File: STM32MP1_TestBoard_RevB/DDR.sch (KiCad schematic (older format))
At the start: 18 parts, among them U1 STM32MP157xAB, U2 MT41K256M16TW-107

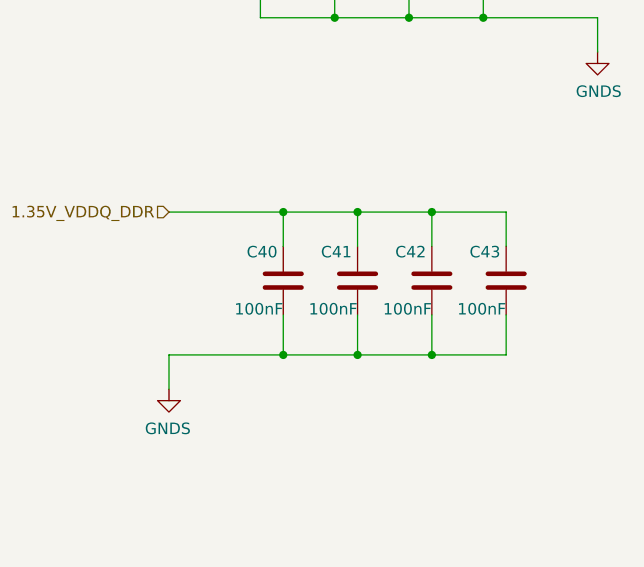
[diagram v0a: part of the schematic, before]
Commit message: Removed 1.35V led and unused DDR capacitors
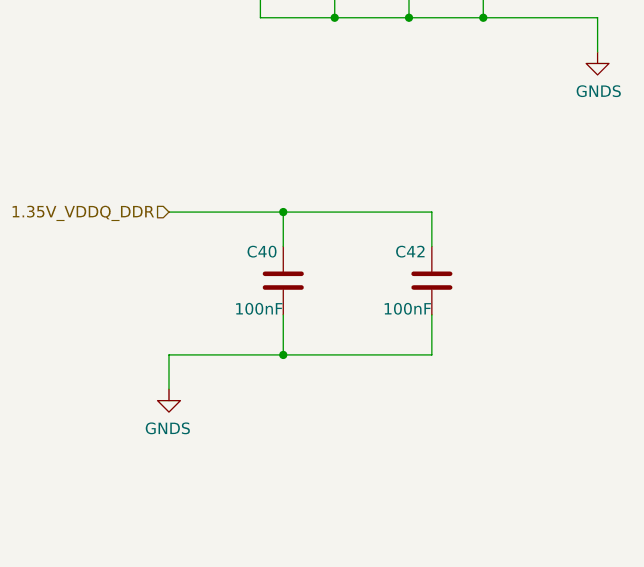
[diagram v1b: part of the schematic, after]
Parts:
- removed C41, C43: 100nF, Capacitor_SMD:C_0402_1005Metric_Pad0.74x0.62mm_HandSolder, symbol Device:C
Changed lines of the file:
@@
 	12825 3425 12500 3425
-Wire Wire Line
-	13250 5050 13250 4900
-$Comp
-L Device:C C43
-U 1 1 60C8F78E
-P 13250 5200
-F 0 "C43" H 13275 5325 50  0000 L CNN
-F 1 "100nF" H 13250 5075 50  0000 L CNN
-F 2 "Capacitor_SMD:C_0402_1005Metric_Pad0.74x0.62mm_HandSolder" H 13288 5050 50  0001 C CNN
-F 3 "~" H 13250 5200 50  0001 C CNN
-F 4 "~" H 13250 5200 50  0001 C CNN "Mfr"
-F 5 "~" H 13250 5200 50  0001 C CNN "PartNo"
-	1    13250 5200
-	-1   0    0    -1
-$EndComp
-Wire Wire Line
-	13250 5350 13250 5525
 Wire Wire Line
 	12925 5050 12925 4900
@@
 	12925 5350 12925 5525
 Wire Wire Line
-	12600 5050 12600 4900
-$Comp
-L Device:C C41
-U 1 1 60C8F79E
-P 12600 5200
-F 0 "C41" H 12625 5325 50  0000 L CNN
-F 1 "100nF" H 12600 5075 50  0000 L CNN
-F 2 "Capacitor_SMD:C_0402_1005Metric_Pad0.74x0.62mm_HandSolder" H 12638 5050 50  0001 C CNN
-F 3 "~" H 12600 5200 50  0001 C CNN
-F 4 "~" H 12600 5200 50  0001 C CNN "Mfr"
-F 5 "~" H 12600 5200 50  0001 C CNN "PartNo"
-	1    12600 5200
-	-1   0    0    -1
-$EndComp
-Wire Wire Line
-	12600 5350 12600 5525
-Wire Wire Line
 	12275 5050 12275 4900
 $Comp
@@
 Wire Wire Line
 	12275 5350 12275 5525
-Wire Wire Line
-	13250 4900 12925 4900
-Connection ~ 12925 4900
-Wire Wire Line
-	12925 4900 12600 4900
-Connection ~ 12600 4900
-Wire Wire Line
-	12600 4900 12275 4900
 Connection ~ 12275 4900
 Wire Wire Line
@@
 Wire Wire Line
 	11775 5525 11775 5675
-Wire Wire Line
-	13250 5525 12925 5525
-Connection ~ 12925 5525
-Wire Wire Line
-	12925 5525 12600 5525
-Connection ~ 12600 5525
-Wire Wire Line
-	12600 5525 12275 5525
 Connection ~ 12275 5525
 Wire Wire Line
@@
 NoConn ~ 4700 5625
 NoConn ~ 4700 5725
+Wire Wire Line
+	12275 5525 12925 5525
+Wire Wire Line
+	12275 4900 12925 4900
 $EndSCHEMATC

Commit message: Updated design
- Added Crystal/Oscillators
- Replaced both SDMMC with single SDMMC w/ detect pin
- Added USB Type C for VIN
- Moved SWD pins
- Tidied up silk screen for pin headers J1, J2, J3, J4
- Moved DSI socket
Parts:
- C36, C40, C42, C52, C57, C62, C65: LCSC (none) -> C1525
- R14: LCSC (none) -> C25076
- R15, R6: LCSC (none) -> C25744
- R2, R52: LCSC (none) -> C11702
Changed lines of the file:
@@
 $Descr A3 16535 11693
 encoding utf-8
-Sheet 6 10
+Sheet 6 9
 Title ""
 Date ""
@@
 F 4 "Micron" H 7675 4325 50  0001 C CNN "Mfr"
 F 5 "MT41K256M16TW-107" H 7675 4325 50  0001 C CNN "PartNo"
+F 6 "~" H 7675 4325 50  0001 C CNN "LCSC"
 	1    7675 4325
 	1    0    0    -1
@@
 F 4 "~" H 1500 8800 50  0001 C CNN "Mfr"
 F 5 "~" H 1500 8800 50  0001 C CNN "PartNo"
+F 6 "C1525" H 1500 8800 50  0001 C CNN "LCSC"
 	1    1500 8800
 	1    0    0    -1
@@
 F 4 "~" H 5750 6100 50  0001 C CNN "Mfr"
 F 5 "~" H 5750 6100 50  0001 C CNN "PartNo"
+F 6 "~" H 5750 6100 50  0001 C CNN "LCSC"
 	1    5750 6100
 	1    0    0    -1
@@
 F 4 "~" H 8750 6075 50  0001 C CNN "Mfr"
 F 5 "~" H 8750 6075 50  0001 C CNN "PartNo"
+F 6 "~" H 8750 6075 50  0001 C CNN "LCSC"
 	1    8750 6075
 	1    0    0    -1
@@
 F 4 "~" H 2325 8800 50  0001 C CNN "Mfr"
 F 5 "~" H 2325 8800 50  0001 C CNN "PartNo"
+F 6 "C25744" H 2325 8800 50  0001 C CNN "LCSC"
 	1    2325 8800
 	1    0    0    -1
@@
 F 4 "~" H 6050 6100 50  0001 C CNN "Mfr"
 F 5 "~" H 6050 6100 50  0001 C CNN "PartNo"
+F 6 "C25744" H 6050 6100 50  0001 C CNN "LCSC"
 	1    6050 6100
 	1    0    0    -1
@@
 F 4 "~" H 4600 8050 50  0001 C CNN "Mfr"
 F 5 "~" H 4600 8050 50  0001 C CNN "PartNo"
+F 6 "C25076" H 4600 8050 50  0001 C CNN "LCSC"
 	1    4600 8050
 	0    1    1    0
@@
 F 4 "~" H 12175 3725 50  0001 C CNN "Mfr"
 F 5 "~" H 12175 3725 50  0001 C CNN "PartNo"
+F 6 "C1525" H 12175 3725 50  0001 C CNN "LCSC"
 	1    12175 3725
 	1    0    0    -1
@@
 F 4 "~" H 12500 3725 50  0001 C CNN "Mfr"
 F 5 "~" H 12500 3725 50  0001 C CNN "PartNo"
+F 6 "C1525" H 12500 3725 50  0001 C CNN "LCSC"
 	1    12500 3725
 	1    0    0    -1
@@
 F 4 "~" H 12825 3725 50  0001 C CNN "Mfr"
 F 5 "~" H 12825 3725 50  0001 C CNN "PartNo"
+F 6 "C1525" H 12825 3725 50  0001 C CNN "LCSC"
 	1    12825 3725
 	1    0    0    -1
@@
 F 4 "~" H 13150 3725 50  0001 C CNN "Mfr"
 F 5 "~" H 13150 3725 50  0001 C CNN "PartNo"
+F 6 "C1525" H 13150 3725 50  0001 C CNN "LCSC"
 	1    13150 3725
 	1    0    0    -1
@@
 F 4 "~" H 12925 5200 50  0001 C CNN "Mfr"
 F 5 "~" H 12925 5200 50  0001 C CNN "PartNo"
+F 6 "C1525" H 12925 5200 50  0001 C CNN "LCSC"
 	1    12925 5200
 	-1   0    0    -1
@@
 F 4 "~" H 12275 5200 50  0001 C CNN "Mfr"
 F 5 "~" H 12275 5200 50  0001 C CNN "PartNo"
+F 6 "C1525" H 12275 5200 50  0001 C CNN "LCSC"
 	1    12275 5200
 	-1   0    0    -1
@@
 F 4 "~" H 4350 9550 50  0001 C CNN "Mfr"
 F 5 "~" H 4350 9550 50  0001 C CNN "PartNo"
+F 6 "C11702" H 4350 9550 50  0001 C CNN "LCSC"
 	1    4350 9550
 	0    -1   1    0
@@
 F 4 "~" H 4925 9550 50  0001 C CNN "Mfr"
 F 5 "~" H 4925 9550 50  0001 C CNN "PartNo"
+F 6 "C11702" H 4925 9550 50  0001 C CNN "LCSC"
 	1    4925 9550
 	0    -1   1    0
@@
 F 4 "~" H 3800 4125 50  0001 C CNN "Mfr"
 F 5 "~" H 3800 4125 50  0001 C CNN "PartNo"
+F 6 "~" H 3800 4125 50  0001 C CNN "LCSC"
 	3    3800 4125
 	1    0    0    -1
